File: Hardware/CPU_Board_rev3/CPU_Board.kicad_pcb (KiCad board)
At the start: 2 copper layers, 100 x 70 mm, 113 parts, among them P1 CONN_01X02, P10 CONN_01X02, P11 CONN_01X02, P12 CONN_01X02, P13 CONN_01X02, P14 CONN_01X06, P15 CONN_01X03, P16 CONN_01X01, P17 CONN_01X03, P18 CONN_01X01, P19 CONN_01X01, P2 USB_B, P20 CONN_01X01, P21 CONN_01X03, P22 CONN_01X01, P23 CONN_01X01, P24 CONN_01X01, P25 CONN_01X01, P3 CONN_01X04, P4 CONN_01X04, P5 CONN_01X04, P6 CONN_01X04, P7 CONN_01X06, P8 CONN_01X06, P9 CONN_01X06, Q1 Q_PMOS_GSD, Q2 Q_PNP_BCE, Q3 Q_PNP_BCE, U1 STM32F411RETx, U10 MCDTS2-4N, U11 MCDTS2-4N, U12 LPS22HB, U13 INA128, U2 FT232RL, U3 NCP1117DT12G, U4 HTS221, U5 INA128, U6 SPBTLE-RF, U7 A2235-H, U8 LSM303AGR, U9 LSM6DSL, Y1 8MHz

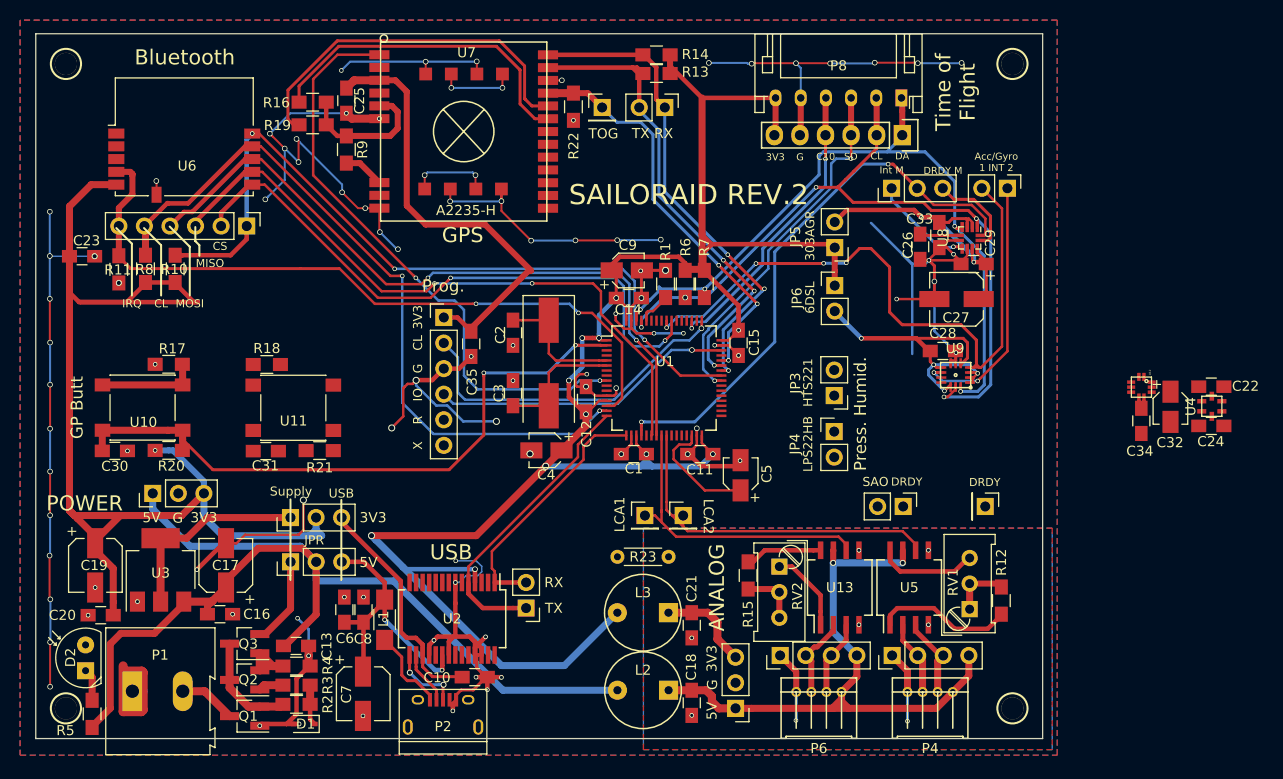
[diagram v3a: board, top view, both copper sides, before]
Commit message: Revision 3 routed and completed
* Schematic completed
* Layout of components complete
* Routing complete
* Excessive via placing complete (All potential antennas, no matter how
slight should have been prevented)
* Gerbers generated
* Drill generated
* A2235 footprint/library fixed
* Minor other adjustments
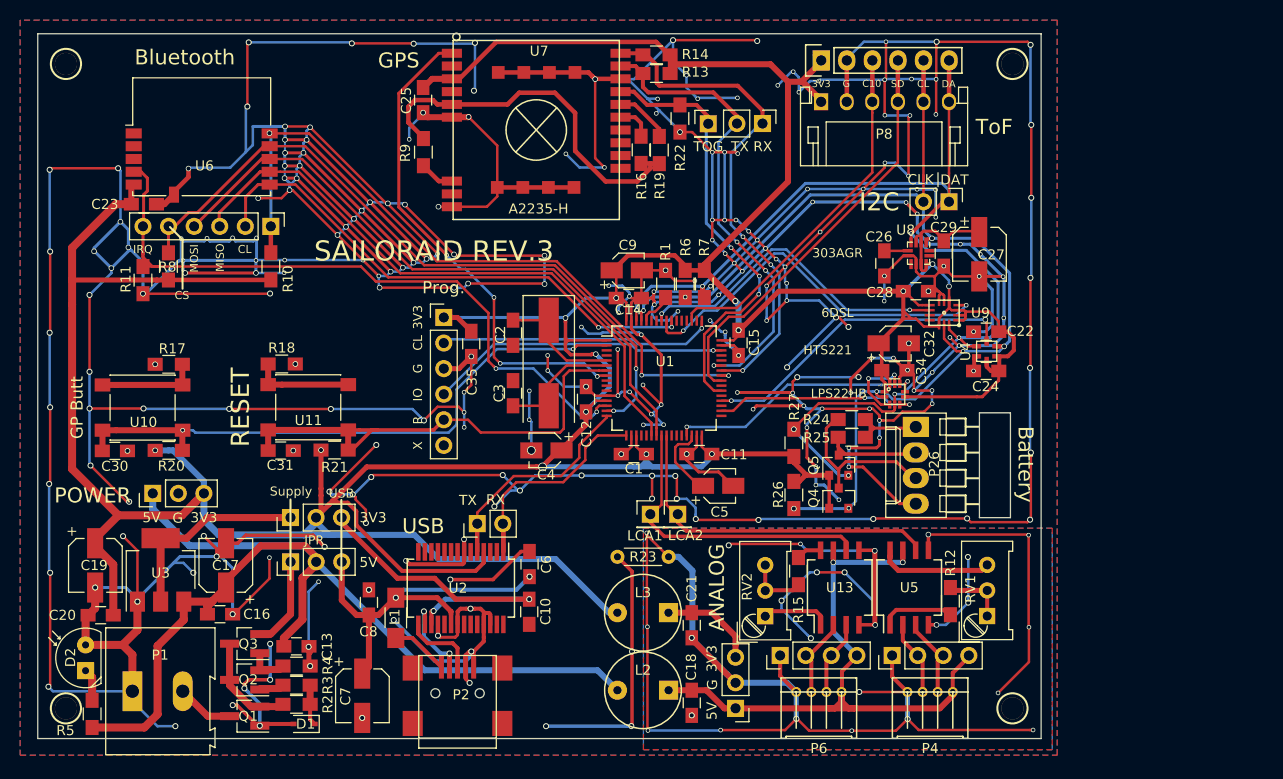
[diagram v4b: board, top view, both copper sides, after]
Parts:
- removed C33: 100nF, Capacitors_SMD:C_0805_HandSoldering
- removed JP3, JP4, JP5, JP6: Jumper_NC_Small, Pin_Headers:Pin_Header_Straight_1x02_Pitch2.54mm
- removed P13: CONN_01X02, Pin_Headers:Pin_Header_Straight_1x02_Pitch2.54mm
- removed P17: CONN_01X03, Pin_Headers:Pin_Header_Straight_1x03_Pitch2.54mm
- removed P18: CONN_01X01, Pin_Headers:Pin_Header_Straight_1x01_Pitch2.54mm
- added P26: CONN_01X04, Connectors_Molex:Molex_KK-6410-04_04x2.54mm_Straight, F.Cu at (130.9, 141.4)
- added Q4: BSS138, TO_SOT_Packages_SMD:SOT-23, F.Cu at (123.3, 148.5)
- added Q5: BSS138, TO_SOT_Packages_SMD:SOT-23, F.Cu at (123.3, 145.2)
- added R24: R, Resistors_SMD:R_0805_HandSoldering, F.Cu at (124.6, 140.7)
- added R25: R, Resistors_SMD:R_0805_HandSoldering, F.Cu at (124.6, 142.4)
- added R26: R, Resistors_SMD:R_0805_HandSoldering, F.Cu at (118.8, 148.2)
- added R27: R, Resistors_SMD:R_0805_HandSoldering, F.Cu at (118.8, 143.0)
- P2: footprint Connectors:USB_Micro-B -> Connectors:USB_Mini-B
- P8: footprint FOOTPRINTS:JST_PH_S6B-PH-K_06x2.50mm_Angled -> FOOTPRINTS:JST_PH_S6B-PH-K_06x2.54mm_Angled
- R6, R7: value 5k -> 10k
- moved R19 34.5 mm to (105.5, 113.9), turned to 90 degrees
- moved R16 33.0 mm to (103.7, 113.9), turned to 90 degrees
- moved C32 28.2 mm to (128.8, 133.1), turned to 0 degrees
- moved C34 25.0 mm to (128.8, 135.8), turned to 0 degrees
- moved U12 24.5 mm to (128.9, 138.2), turned to 180 degrees
- moved C22 23.0 mm to (137.9, 131.9)
- moved C24 23.0 mm to (137.9, 135.8)
- moved U4 23.0 mm to (138.0, 133.9)
- moved C6 18.9 mm to (92.6, 155.0)
- moved P7 10.9 mm to (121.6, 105.0), turned to 0 degrees
- moved P16 10.7 mm to (110.3, 111.3)
- moved R22 10.6 mm to (107.5, 110.8)
- moved P11 9.84 mm to (115.7, 111.3)
- moved P10 9.68 mm to (87.4, 151.0), turned to 90 degrees
- moved R10 9.50 mm to (66.9, 125.5)
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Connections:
- net /LPS_DRDY renamed /LPS_I_DRDY
- C22 pad 1: /HTS_VDD -> +3V3
- C24 pad 1: /HTS_VDD -> +3V3
- C27 pad 1: /LSM303_VDD -> +3V3
- C28 pad 1: /LSM6_VDD -> +3V3
- C29 pad 1: /LSM303_VDD -> +3V3
- C32 pad 1: /LPS_VDD -> +3V3
- C34 pad 1: /LPS_VDD -> +3V3
- P12 pad 1: /LSM6DSL_INT2 -> /IMU_I2C_DA
- P12 pad 2: /LSM6DSL_INT1 -> /IMU_I2C_CL
- P22 pad 1: (no net) -> Net-(P22-Pad1)
- P23 pad 1: (no net) -> Net-(P23-Pad1)
- P24 pad 1: (no net) -> Net-(P24-Pad1)
- P25 pad 1: (no net) -> Net-(P25-Pad1)
- P7 pad 1: /IMU_I2C_DA -> +3V3
- P7 pad 2: /IMU_I2C_CL -> GND
- P7 pad 3: /VL_C9 -> /VL_C10
- P7 pad 4: /VL_C10 -> /TOF_SD
- P7 pad 5: GND -> /IMU_I2C_CL
- P7 pad 6: +3V3 -> /IMU_I2C_DA
- P8 pad 1: /IMU_I2C_DA -> +3V3
- P8 pad 2: /IMU_I2C_CL -> GND
- P8 pad 3: /VL_C9 -> /VL_C10
- P8 pad 4: /VL_C10 -> /TOF_SD
- P8 pad 5: GND -> /IMU_I2C_CL
- P8 pad 6: +3V3 -> /IMU_I2C_DA
- P9 pad 6: (no net) -> Net-(P9-Pad6)
- U1 pad 10: (no net) -> Net-(U1-Pad10)
- U1 pad 11: (no net) -> Net-(U1-Pad11)
- U1 pad 20: /303C_I_XL -> Net-(U1-Pad20)
- U1 pad 21: /INT_Mag -> Net-(U1-Pad21)
- U1 pad 26: /DRDY_Mag -> Net-(U1-Pad26)
- U1 pad 27: (no net) -> Net-(U1-Pad27)
- U1 pad 28: (no net) -> Net-(U1-Pad28)
- U1 pad 3: (no net) -> Net-(U1-Pad3)
- U1 pad 33: (no net) -> Net-(U1-Pad33)
- U1 pad 35: (no net) -> Net-(U1-Pad35)
- U1 pad 37: (no net) -> Net-(U1-Pad37)
- U1 pad 39: (no net) -> Net-(U1-Pad39)
- U1 pad 4: (no net) -> Net-(U1-Pad4)
- U1 pad 40: /VL_C9 -> /TOF_SD
- U1 pad 44: (no net) -> Net-(U1-Pad44)
- U1 pad 45: (no net) -> Net-(U1-Pad45)
- U1 pad 50: (no net) -> Net-(U1-Pad50)
- U1 pad 52: (no net) -> Net-(U1-Pad52)
- U1 pad 53: (no net) -> Net-(U1-Pad53)
- U1 pad 54: (no net) -> Net-(U1-Pad54)
- U1 pad 58: (no net) -> Net-(U1-Pad58)
- U1 pad 59: (no net) -> Net-(U1-Pad59)
- U1 pad 9: (no net) -> Net-(U1-Pad9)
- U12 pad 1: /LPS_VDD -> +3V3
- U12 pad 10: /LPS_VDD -> +3V3
- U12 pad 6: /LPS_VDD -> +3V3
- U2 pad 10: (no net) -> Net-(U2-Pad10)
- U2 pad 11: (no net) -> Net-(U2-Pad11)
- U2 pad 12: (no net) -> Net-(U2-Pad12)
- U2 pad 13: (no net) -> Net-(U2-Pad13)
- U2 pad 14: (no net) -> Net-(U2-Pad14)
- U2 pad 19: (no net) -> Net-(U2-Pad19)
- U2 pad 2: (no net) -> Net-(U2-Pad2)
- U2 pad 22: (no net) -> Net-(U2-Pad22)
- U2 pad 23: (no net) -> Net-(U2-Pad23)
- U2 pad 27: (no net) -> Net-(U2-Pad27)
- U2 pad 28: (no net) -> Net-(U2-Pad28)
- U2 pad 3: (no net) -> Net-(U2-Pad3)
- U2 pad 6: (no net) -> Net-(U2-Pad6)
- U2 pad 9: (no net) -> Net-(U2-Pad9)
- U4 pad 1: /HTS_VDD -> +3V3
- U4 pad 6: /HTS_VDD -> +3V3
- U6 pad 1: (no net) -> Net-(U6-Pad1)
- U6 pad 2: (no net) -> Net-(U6-Pad2)
- U6 pad 3: (no net) -> Net-(U6-Pad3)
- U7 pad 10: (no net) -> Net-(U7-Pad10)
- U7 pad 11: (no net) -> Net-(U7-Pad11)
- U7 pad 12: (no net) -> Net-(U7-Pad12)
- U7 pad 13: (no net) -> Net-(U7-Pad13)
- U7 pad 14: (no net) -> Net-(R16-Pad2)
- U7 pad 15: (no net) -> Net-(R19-Pad2)
- U7 pad 16: (no net) -> /GPS_TOGGLE
- U7 pad 17: Net-(R16-Pad2) -> GND
- U7 pad 18: Net-(R19-Pad2) -> /GPS_TX
- U7 pad 19: /GPS_TOGGLE -> /GPS_RX
- U7 pad 2: (no net) -> Net-(U7-Pad2)
- U7 pad 21: /GPS_TX -> GND
- U7 pad 22: /GPS_RX -> GND
- U7 pad 4: (no net) -> Net-(U7-Pad4)
- U7 pad 8: (no net) -> Net-(U7-Pad8)
- U8 pad 10: /LSM303_VDD -> +3V3
- U8 pad 11: /DRDY_Mag -> Net-(U8-Pad11)
- U8 pad 12: /303C_I_XL -> Net-(U8-Pad12)
- U8 pad 2: /LSM303_VDD -> +3V3
- U8 pad 3: /LSM303_VDD -> +3V3
- U8 pad 7: /INT_Mag -> /INT/DRDY_Mag
- U8 pad 9: /LSM303_VDD -> +3V3
- U9 pad 1: /LSM6_VDD -> +3V3
- U9 pad 10: (no net) -> Net-(U9-Pad10)
- U9 pad 11: (no net) -> Net-(U9-Pad11)
- U9 pad 12: /LSM6_VDD -> +3V3
- U9 pad 2: /LSM6_VDD -> +3V3
- U9 pad 3: /LSM6_VDD -> +3V3
- U9 pad 5: /LSM6_VDD -> +3V3
- U9 pad 8: /LSM6_VDD -> +3V3
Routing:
- net GND: track 386.7 -> 1311.5 mm, vias 98 -> 264
- net GNDA: track 14.3 -> 192.7 mm, vias 8 -> 26
- net +3V3: track 355.6 -> 478.3 mm, vias 12 -> 14
- net /303C_I_XL: track 56.7 -> 0.00 mm, vias 2 -> 0
- net /NRST: track 0.00 -> 47.9 mm
- net /TOF_SD: track 0.00 -> 41.4 mm
- net /IMU_I2C_DA: track 74.4 -> 113.2 mm, vias 4 -> 7
- net /VL_C9: track 36.0 -> 0.00 mm, vias 2 -> 0
- net /LSM6_VDD: track 34.0 -> 0.00 mm, vias 4 -> 0
- net /IMU_I2C_CL: track 76.5 -> 110.2 mm, vias 5 -> 8
- net /LSM303_VDD: track 32.7 -> 0.00 mm, vias 2 -> 0
- net /HTS_DRDY: track 0.00 -> 31.7 mm, vias 0 -> 2
- net Net-(R19-Pad2): track 36.7 -> 5.60 mm
- net Net-(R16-Pad2): track 32.9 -> 3.58 mm
- net /LSM6DSL_INT1: track 65.5 -> 37.9 mm, vias 4 -> 2
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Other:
- board size 100 x 70 mm -> 99.7 x 70 mm
- board text added: "Battery"
- board text added: "CLK"
- board text added: "DAT"
- board text added: "I2C"
- board text added: "RESET"
- board text added: "SAILORAID REV.3"
- board text added: "ToF"
- board text removed: "Acc/Gyro 1 INT 2"
- board text removed: "DRDY"
- board text removed: "DRDY M"
- board text removed: "Int M"
- board text removed: "Press. Humid."
- board text removed: "SAILORAID REV.2"
- board text removed: "SAO"
- board text removed: "Time of Flight"

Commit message: last fixes
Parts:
- U13, U5: footprint Housings_SOIC:SO-8_5.3x6.2mm_Pitch1.27mm -> Housings_SOIC:SOIC-8_3.9x4.9mm_Pitch1.27mm
- moved R12 0.26 mm to (134.1, 158.7)
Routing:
- net GNDA: track 192.7 -> 200.4 mm, vias 26 -> 28
- net /GPS_Vout: track 37.4 -> 42.1 mm
- net GND: track 1311.5 -> 1313.5 mm, vias 264 -> 267
- net +5VA: track 62.9 -> 61.6 mm
- net Net-(P3-Pad2): track 7.49 -> 8.68 mm
- net Net-(P5-Pad3): track 7.49 -> 8.49 mm
- net Net-(P5-Pad2): track 8.24 -> 9.24 mm
- net /Load_cell_amp_2: track 34.3 -> 35.3 mm
- net /Load_cell_amp_1: track 30.3 -> 31.3 mm
- net Net-(R12-Pad1): track 7.32 -> 8.31 mm
- net Net-(P3-Pad3): track 8.29 -> 9.22 mm
- net Net-(RV2-Pad1): track 6.79 -> 5.89 mm

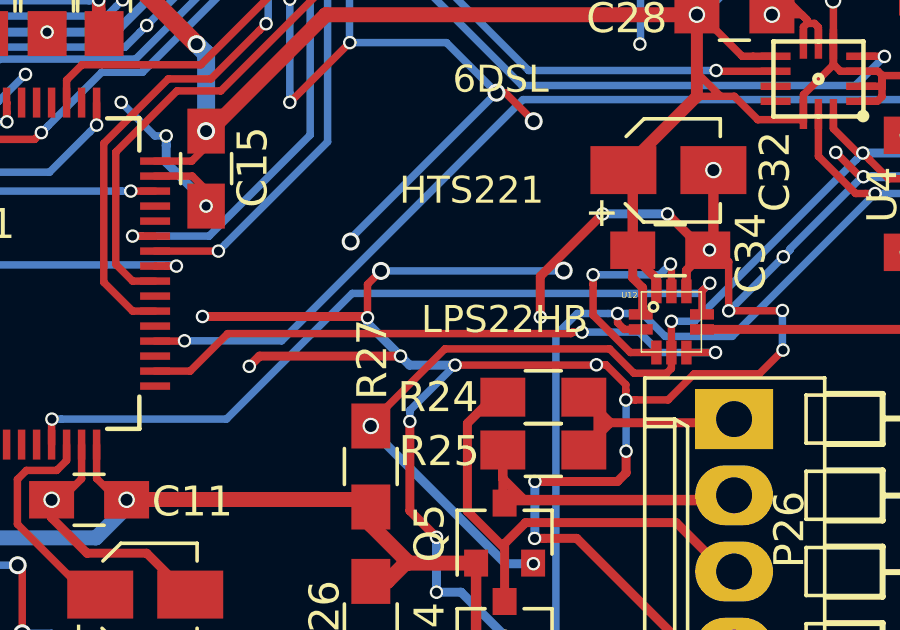
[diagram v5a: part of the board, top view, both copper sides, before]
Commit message: Added appendix to report, fixed last error in pcb layout (missing junction)
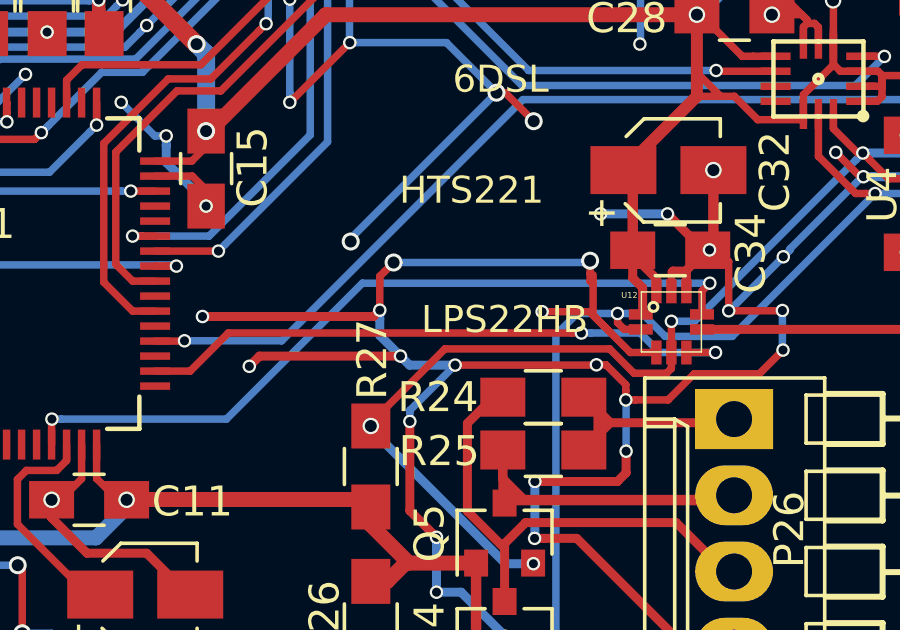
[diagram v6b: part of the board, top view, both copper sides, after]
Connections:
- U12 pad 3: Net-(U12-Pad3) -> GND
- U12 pad 9: Net-(U12-Pad3) -> GND
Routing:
- net Net-(U12-Pad3): track 7.63 -> 0.00 mm, vias 2 -> 0
- net GND: track 1313.5 -> 1318.7 mm

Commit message: Some HW report done..
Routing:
- net GND: track 1318.7 -> 1313.7 mm
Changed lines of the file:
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@@
     (links 303)
     (no_connects 0)
-    (area 43.699999 102.299999 143.450001 172.400018)
+    (area 35.047619 100.975 145.533334 176.425)
     (thickness 1.6)
     (drawings 86)
-    (tracks 2213)
+    (tracks 2211)
     (zones 0)
     (modules 112)
@@
   )
   (setup
-    (last_trace_width 0.25)
+    (last_trace_width 0.15)
     (user_trace_width 0.25)
     (user_trace_width 0.3)
@@
   (segment (start 130.73 124.4) (end 130.98 124.65) (width 0.25) (layer F.Cu) (net 1))
   (segment (start 130.98 124.65) (end 130.98 125.225) (width 0.25) (layer F.Cu) (net 1))
-  (segment (start 89.385 113.465) (end 89.385 117.615) (width 0.25) (layer F.Cu) (net 1))
-  (segment (start 89.385 118.5) (end 89.385 117.615) (width 0.25) (layer F.Cu) (net 1))
   (via (at 98.2 137.4) (size 0.55) (drill 0.4) (layers F.Cu B.Cu) (net 1))
   (segment (start 100.25 138.3) (end 99.1 138.3) (width 0.25) (layer F.Cu) (net 1))
